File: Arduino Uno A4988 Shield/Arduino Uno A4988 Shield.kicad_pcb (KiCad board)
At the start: 2 copper layers, 68.6 x 53.3 mm, 8 parts, among them J1 Power, J2 Digital/PWM, J3 Analog, J4 Digital/PWM

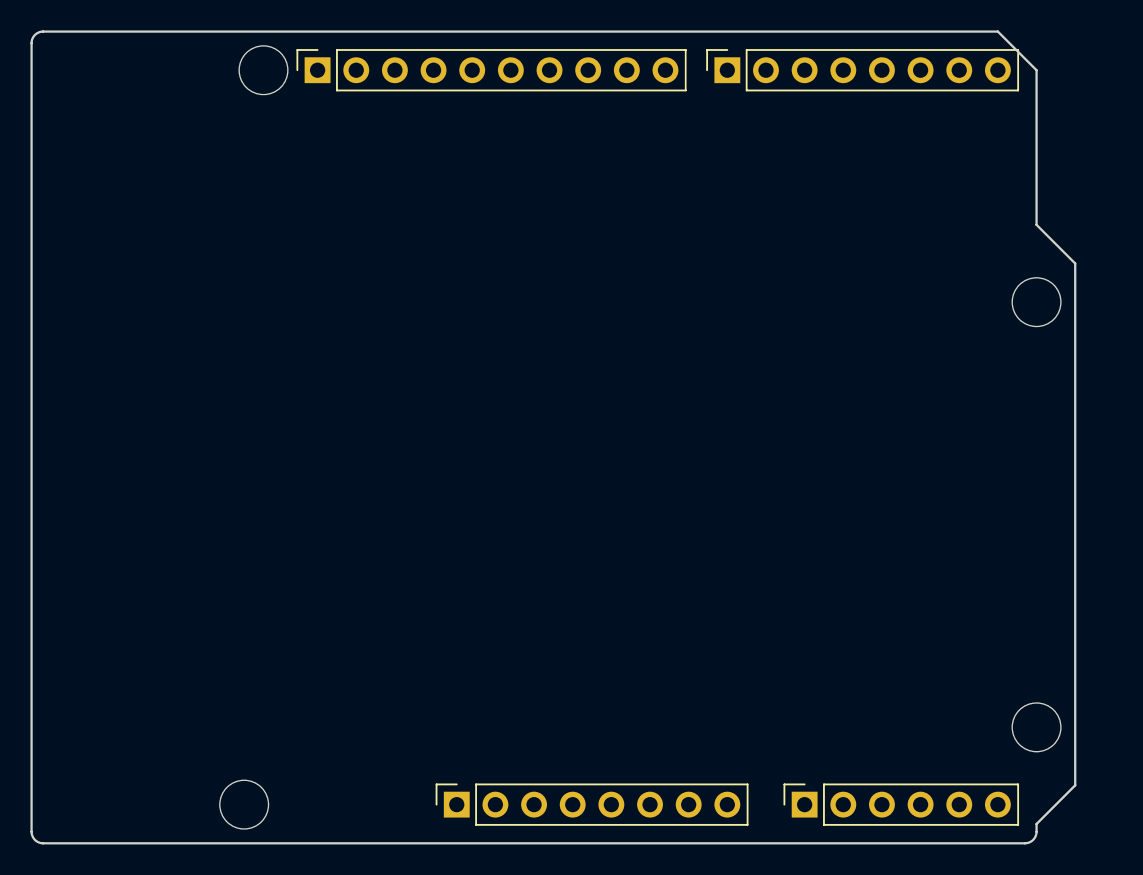
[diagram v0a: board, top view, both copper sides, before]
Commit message: Completed Shaorong and A4988 Shield
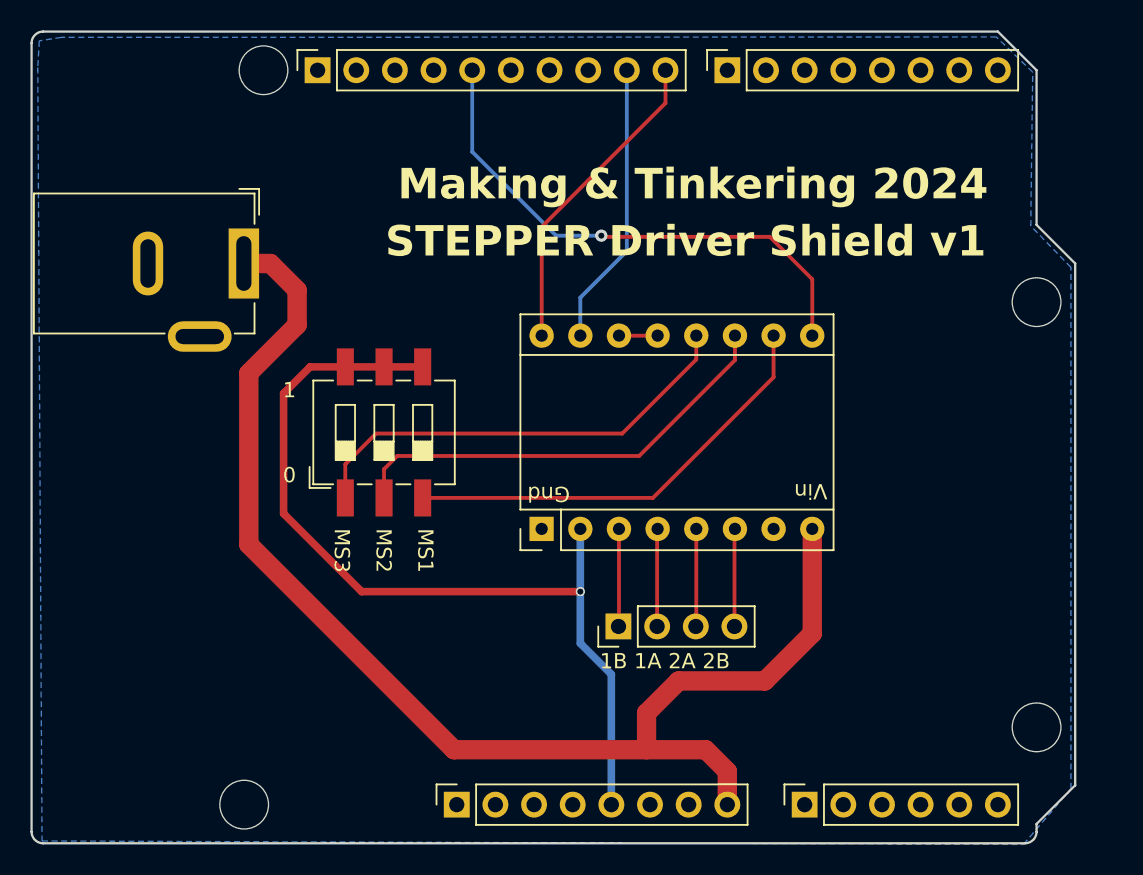
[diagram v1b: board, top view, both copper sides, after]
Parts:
- added A1: Pololu_Breakout_A4988, Module:Pololu_Breakout-16_15.2x20.3mm, F.Cu at (133.5, 79.3)
- added J5: Conn_01x04, Connector_PinHeader_2.54mm:PinHeader_1x04_P2.54mm_Vertical, F.Cu at (138.6, 85.8)
- added J7: Barrel_Jack_Switch_Pin3Ring, Connector_BarrelJack:BarrelJack_GCT_DCJ200-10-A_Horizontal, F.Cu at (114.0, 61.9)
- added SW1: SW_DIP_x03, Button_Switch_SMD:SW_DIP_SPSTx03_Slide_6.7x9.18mm_W8.61mm_P2.54mm_LowProfile, F.Cu at (123.2, 73.0)
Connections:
- J1 pad 8: VCC -> +12V
- J2 pad 1: /SCL/A5 -> unconnected-(J2-Pin_1-Pad1)
- J2 pad 2: /SDA/A4 -> unconnected-(J2-Pin_2-Pad2)
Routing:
- net +12V: track 0.00 -> 84.4 mm
- net +5V: track 0.00 -> 58.3 mm, vias 0 -> 1
- net /13: track 0.00 -> 34.9 mm, vias 0 -> 1
- net Net-(A1-MS3): track 0.00 -> 29.7 mm
- net Net-(A1-MS2): track 0.00 -> 29.5 mm
- net Net-(A1-MS1): track 0.00 -> 29.1 mm
- net /8: track 0.00 -> 20.8 mm
- net /*9: track 0.00 -> 18.7 mm
- net Net-(A1-2B): track 0.00 -> 6.42 mm
- net Net-(A1-2A): track 0.00 -> 6.42 mm
- net Net-(A1-1A): track 0.00 -> 6.42 mm
- net Net-(A1-1B): track 0.00 -> 6.42 mm
- net Net-(A1-~{RESET}): track 0.00 -> 2.54 mm
- added copper zone on B.Cu, net GND
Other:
- board text added: "0"
- board text added: "1"
- board text added: "1B 1A 2A 2B"
- board text added: "Designed by Jeremy Choo"
- board text added: "Gnd"
- board text added: "MS1"
- board text added: "MS2"
- board text added: "MS3"
- board text added: "Making & Tinkering 2024"
- board text added: "STEPPER Driver Shield v1"
- board text added: "Vin"
- board text removed: "ICSP"
